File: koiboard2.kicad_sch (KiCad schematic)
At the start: 137 parts, among them J1 Conn_01x04, J2 USB_C_Receptacle_USB2.0_16P, J3 Conn_01x05, SW1 choc_v1_SW_HS, SW10 choc_v1_SW_HS, SW11 choc_v1_SW_HS, SW12 choc_v1_SW_HS, SW13 choc_v1_SW_HS, SW14 choc_v1_SW_HS, SW15 choc_v1_SW_HS, SW16 choc_v1_SW_HS, SW17 choc_v1_SW_HS, SW18 choc_v1_SW_HS, SW19 choc_v1_SW_HS, SW2 choc_v1_SW_HS, SW20 choc_v1_SW_HS, SW21 choc_v1_SW_HS, SW22 choc_v1_SW_HS, SW23 choc_v1_SW_HS, SW24 choc_v1_SW_HS, SW25 choc_v1_SW_HS, SW26 choc_v1_SW_HS, SW27 choc_v1_SW_HS, SW28 choc_v1_SW_HS, SW29 choc_v1_SW_HS, SW3 choc_v1_SW_HS, SW30 choc_v1_SW_HS, SW31 choc_v1_SW_HS, SW32 choc_v1_SW_HS, SW33 choc_v1_SW_HS, SW34 choc_v1_SW_HS, SW35 choc_v1_SW_HS, SW36 choc_v1_SW_HS, SW37 choc_v1_SW_HS, SW38 choc_v1_SW_HS, SW39 choc_v1_SW_HS, SW4 choc_v1_SW_HS, SW40 choc_v1_SW_HS, SW41 choc_v1_SW_HS, SW42 choc_v1_SW_HS, SW43 choc_v1_SW_HS, SW44 choc_v1_SW_HS, SW45 choc_v1_SW_HS, SW46 choc_v1_SW_HS, SW47 choc_v1_SW_HS, SW5 choc_v1_SW_HS, SW6 choc_v1_SW_HS, SW7 choc_v1_SW_HS, SW8 choc_v1_SW_HS, SW9 choc_v1_SW_HS, U1 XC6206PxxxMR, U2 SRV05-4, U3 RP2040, U4 W25Q128JVS, Y1 Crystal_GND24

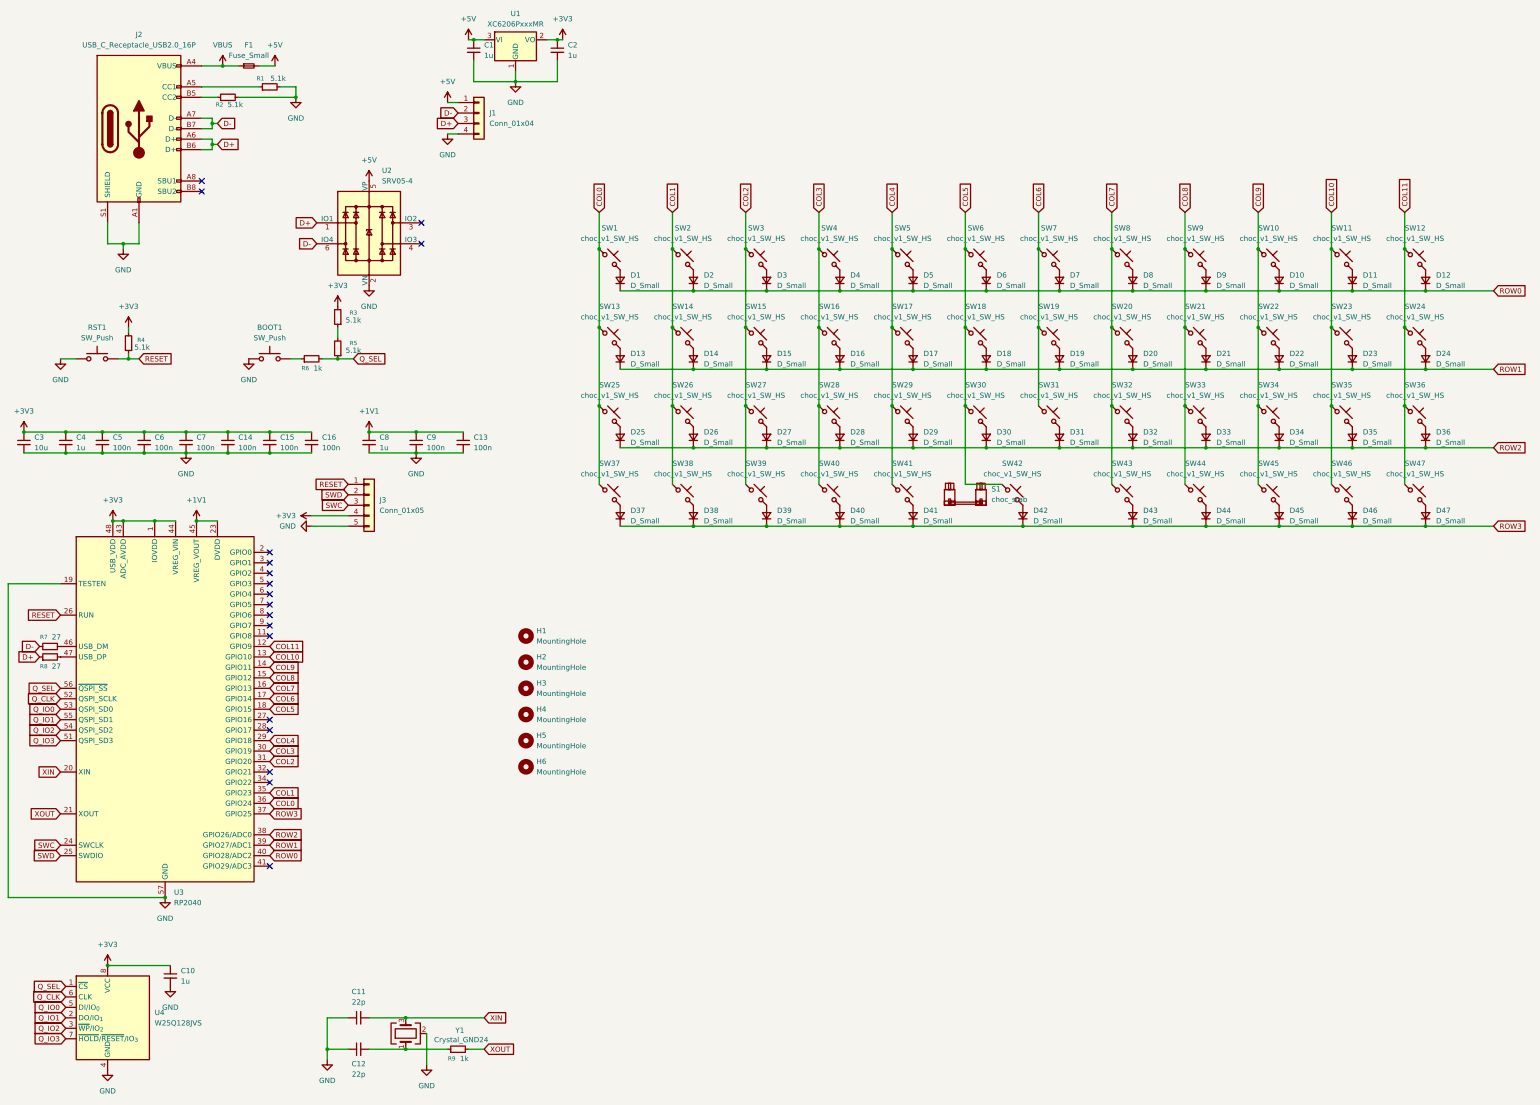
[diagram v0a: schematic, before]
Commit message: update
new 3d files, stab removed, logo moved, 2x1u <-> 2u support, cleanup, pcb dxf, ect...
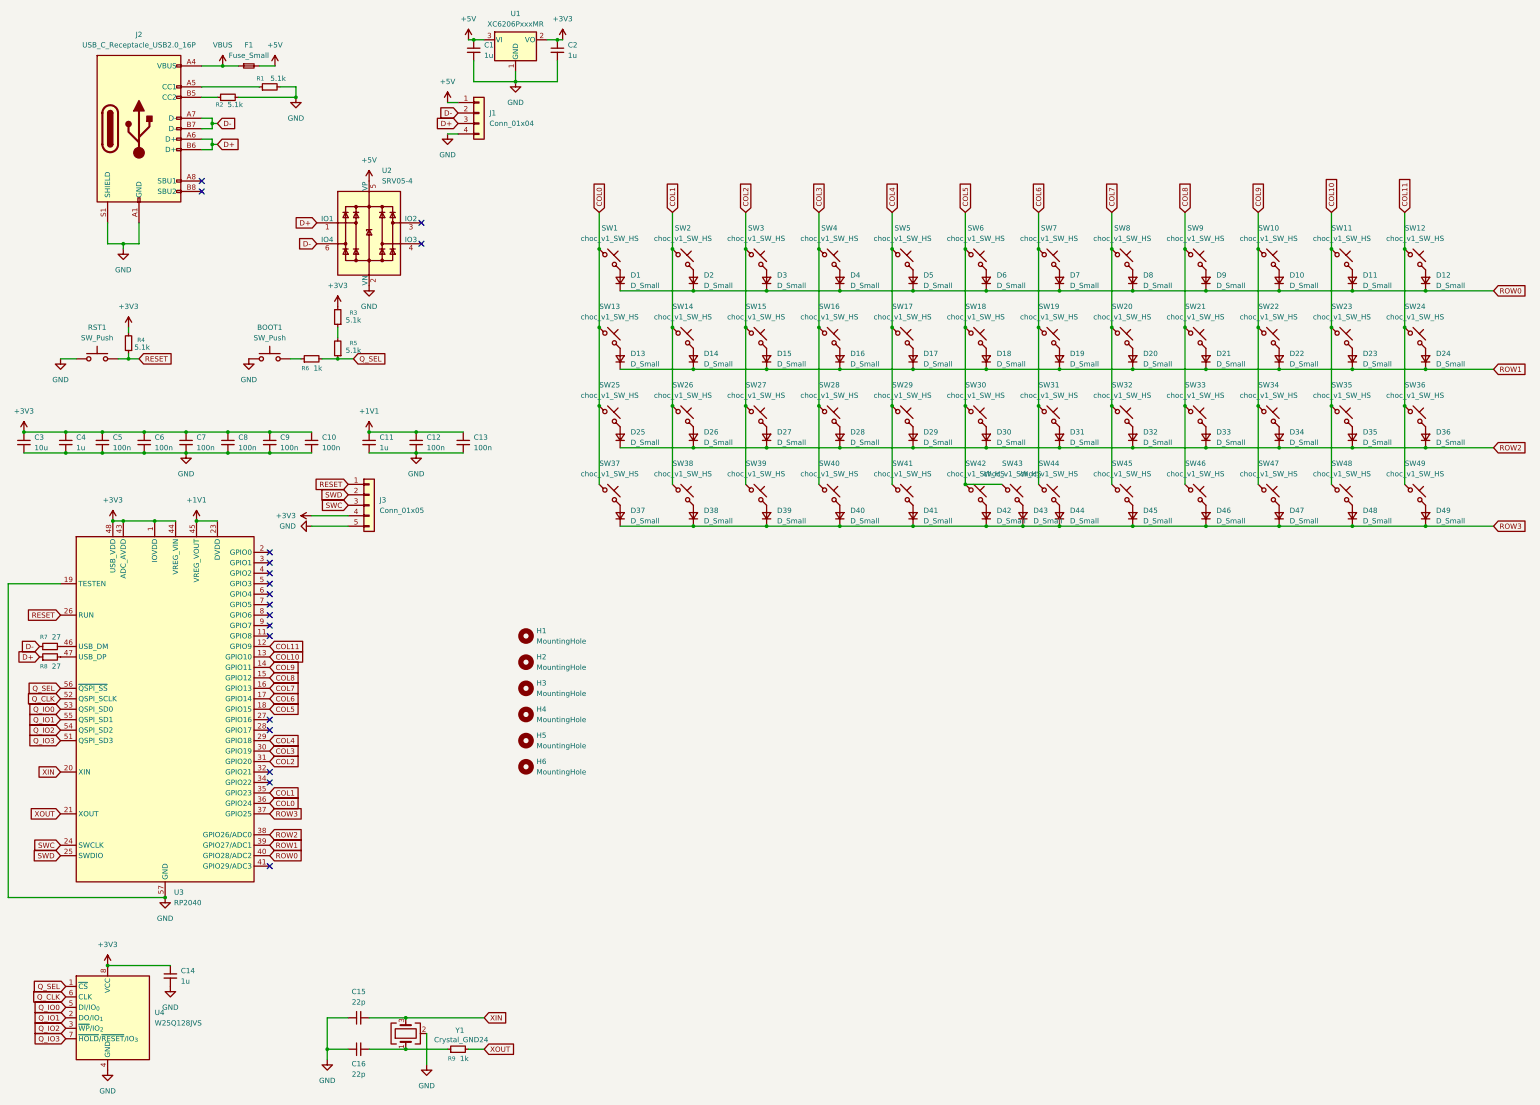
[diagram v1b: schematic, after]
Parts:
- removed S1: choc_stab, PCM_marbastlib-xp-choc:STAB_choc_2u, symbol PCM_marbastlib-choc:choc_stab
- added D43, D44: D_Small, Diode_SMD:D_SOD-123, symbol Device:D_Small
- added SW43: choc_v1_SW_HS, PCM_marbastlib-xp-choc:SW_choc_v2_HS_CPG135001S30_1u, symbol PCM_marbastlib-choc:choc_v1_SW_HS_CPG135001S30
- added SW44: choc_v1_SW_HS, Cool Library:SW_choc_v2_HS_CPG135001S30_1u_switch_hide, symbol PCM_marbastlib-choc:choc_v1_SW_HS_CPG135001S30
- J3: footprint Connector_PinHeader_2.54mm:PinHeader_1x05_P2.54mm_Vertical -> Cool Library:PinHeader_1x05_P2.54mm_Vertical_No_3D_Header
- SW42: footprint PCM_marbastlib-xp-choc:SW_choc_v2_HS_CPG135001S30_1u -> Cool Library:SW_choc_v2_HS_CPG135001S30_1u_switch_hide
- renumbered C16 to C10, C8 to C11, C9 to C12, C10 to C14, C11 to C15, C12 to C16, C14 to C8, C15 to C9, D43 to D45, D44 to D46, D45 to D47, D46 to D48, D47 to D49, SW43 to SW45, SW44 to SW46, SW45 to SW47, SW46 to SW48, SW47 to SW49
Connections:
- net COL5: now also SW43.1
- net COL6: now also SW44.1
- net ROW3: now also D43.1 (K), D44.1 (K)
- new net: D44.2 (A), SW44.2
- new net: D43.2 (A), SW43.2
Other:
- moved on the sheet: D42, SW42

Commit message: update from review
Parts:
- removed BOOT1, RST1: SW_Push, Button_Switch_SMD:SW_SPST_TL3342, symbol Switch:SW_Push
- removed C1, C11, C14, C2, C4: 1u, Capacitor_SMD:C_0402_1005Metric, symbol Device:C_Small
- removed C10, C12, C13, C5, C6, C7, C8, C9: 100n, Capacitor_SMD:C_0402_1005Metric, symbol Device:C_Small
- removed C15, C16: 22p, Capacitor_SMD:C_0402_1005Metric, symbol Device:C_Small
- removed C3: 10u, Capacitor_SMD:C_0603_1608Metric, symbol Device:C_Small
- removed D1, D10, D11, D12, D13, D14, D15, D16, D17, D18, D19, D2, D20, D21, D22, D23, D24, D25, D26, D27, D28, D29, D3, D30, D31, D32, D33, D34, D35, D36, D37, D38, D39, D4, D40, D41, D42, D43, D44, D45, D46, D47, D48, D49, D5, D6, D7, D8, D9: D_Small, Diode_SMD:D_SOD-123, symbol Device:D_Small
- removed F1: Fuse_Small, Fuse:Fuse_1206_3216Metric, symbol Device:Fuse_Small
- removed J1: Conn_01x04, Connector_JST:JST_SH_SM04B-SRSS-TB_1x04-1MP_P1.00mm_Horizontal, symbol Connector_Generic:Conn_01x04
- removed J2: USB_C_Receptacle_USB2.0_16P, Connector_USB:USB_C_Receptacle_HRO_TYPE-C-31-M-12, symbol Connector:USB_C_Receptacle_USB2.0_16P
- removed R1, R2, R3, R4, R5: 5.1k, Resistor_SMD:R_0402_1005Metric, symbol Device:R_Small
- removed R6, R9: 1k, Resistor_SMD:R_0402_1005Metric, symbol Device:R_Small
- removed R7, R8: 27, Resistor_SMD:R_0402_1005Metric, symbol Device:R_Small
- removed SW1, SW10, SW11, SW12, SW13, SW14, SW15, SW16, SW17, SW18, SW19, SW2, SW20, SW21, SW22, SW23, SW24, SW25, SW26, SW27, SW28, SW29, SW3, SW30, SW31, SW32, SW33, SW34, SW35, SW36, SW37, SW38, SW39, SW4, SW40, SW41, SW43, SW45, SW46, SW47, SW48, SW49, SW5, SW6, SW7, SW8, SW9: choc_v1_SW_HS, PCM_marbastlib-xp-choc:SW_choc_v2_HS_CPG135001S30_1u, symbol PCM_marbastlib-choc:choc_v1_SW_HS_CPG135001S30
- removed SW42, SW44: choc_v1_SW_HS, Cool Library:SW_choc_v2_HS_CPG135001S30_1u_switch_hide, symbol PCM_marbastlib-choc:choc_v1_SW_HS_CPG135001S30
- removed U1: XC6206PxxxMR, Package_TO_SOT_SMD:SOT-23-3, symbol Regulator_Linear:XC6206PxxxMR
- removed U2: SRV05-4, PCM_marbastlib-various:SOT-23-6-routable, symbol PCM_marbastlib-various:SRV05-4
- removed U3: RP2040, Package_DFN_QFN:QFN-56-1EP_7x7mm_P0.4mm_EP3.2x3.2mm, symbol MCU_RaspberryPi:RP2040
- removed U4: W25Q128JVS, Package_SO:SOIC-8_5.3x5.3mm_P1.27mm, symbol Memory_Flash:W25Q128JVS
- removed Y1: Crystal_GND24, Crystal:Crystal_SMD_3225-4Pin_3.2x2.5mm, symbol Device:Crystal_GND24
- H1, H2, H3, H4, H5, H6: footprint MountingHole:MountingHole_3.2mm_M3_ISO14580 -> Library:MountingHole_3.2mm_M3_ISO14580
- J3: footprint Cool Library:PinHeader_1x05_P2.54mm_Vertical_No_3D_Header -> Library:PinHeader_1x05_P2.54mm_Vertical_No_3D_Header
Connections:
- no-connect marks 18 -> 0
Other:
- added sheet Crystal (crystal.kicad_sch)
- added sheet Flash memory (flash_memory.kicad_sch)
- added sheet Matrix (matrix.kicad_sch)
- added sheet RP2040 microprocessor (processor.kicad_sch)
- added sheet Reset and boot buttons (buttons.kicad_sch)
- added sheet USB-C connector (usbc.kicad_sch)
- moved on the sheet: H1, H2, H3, H4, H5, H6, J3

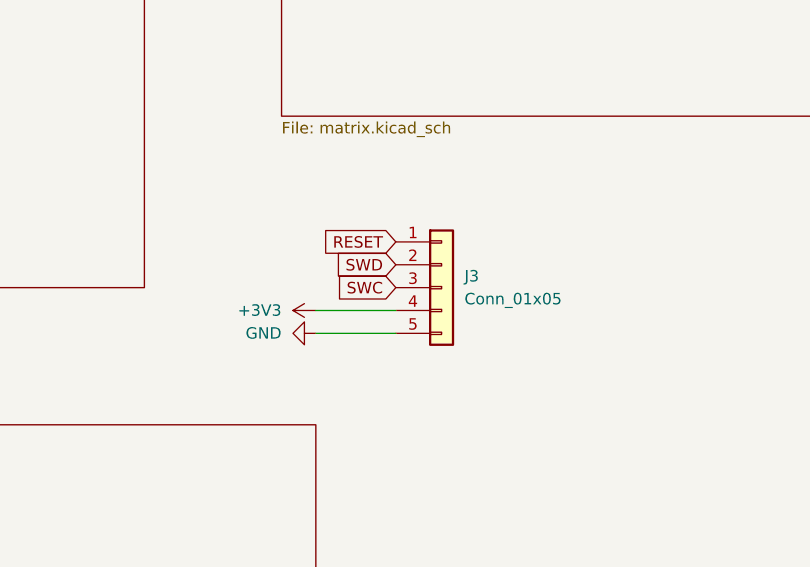
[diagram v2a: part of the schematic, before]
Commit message: 4 layers
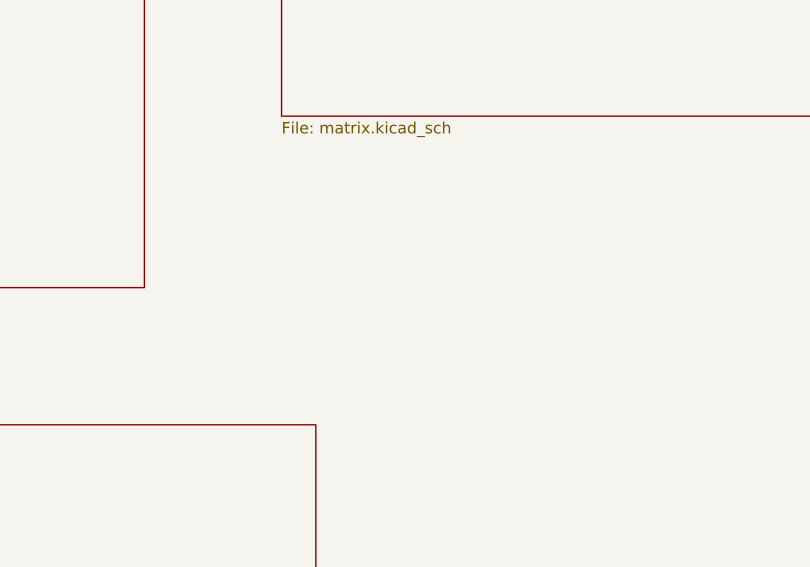
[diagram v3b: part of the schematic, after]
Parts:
- removed J3: Conn_01x05, Library:PinHeader_1x05_P2.54mm_Vertical_No_3D_Header, symbol Connector_Generic:Conn_01x05
